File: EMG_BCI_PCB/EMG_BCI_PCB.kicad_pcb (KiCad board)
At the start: 2 copper layers, 94 x 66 mm, 93 parts, among them J1 Conn_01x03, J2 Conn_01x02, J3 Conn_01x03_Male, Q1 Q_PNP_Darlington_BCE, U1 TL072, U2 INA827, U3 ADA4807-4, U4 ADA4807-4, U5 ADS1013IDGS, U6 TC1044S, U7 LM2776

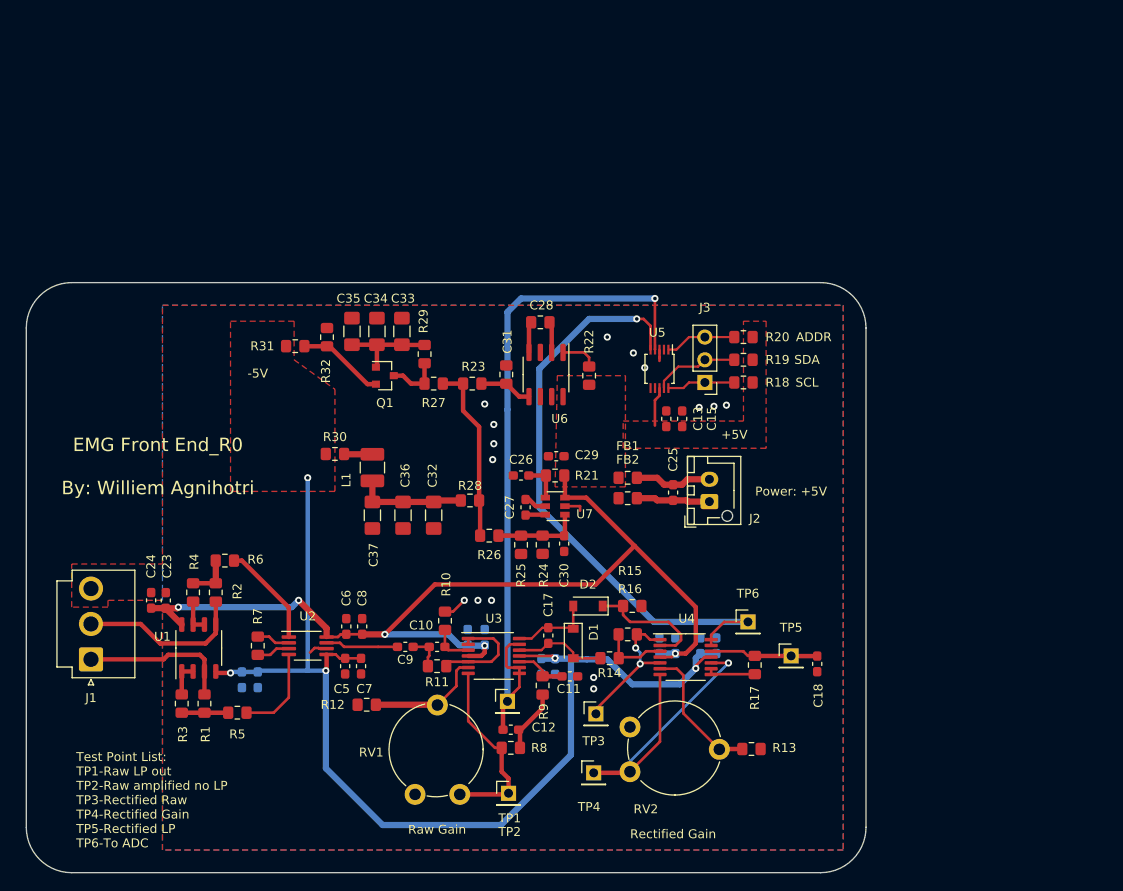
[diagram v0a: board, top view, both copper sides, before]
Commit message: Imported footprints into layout
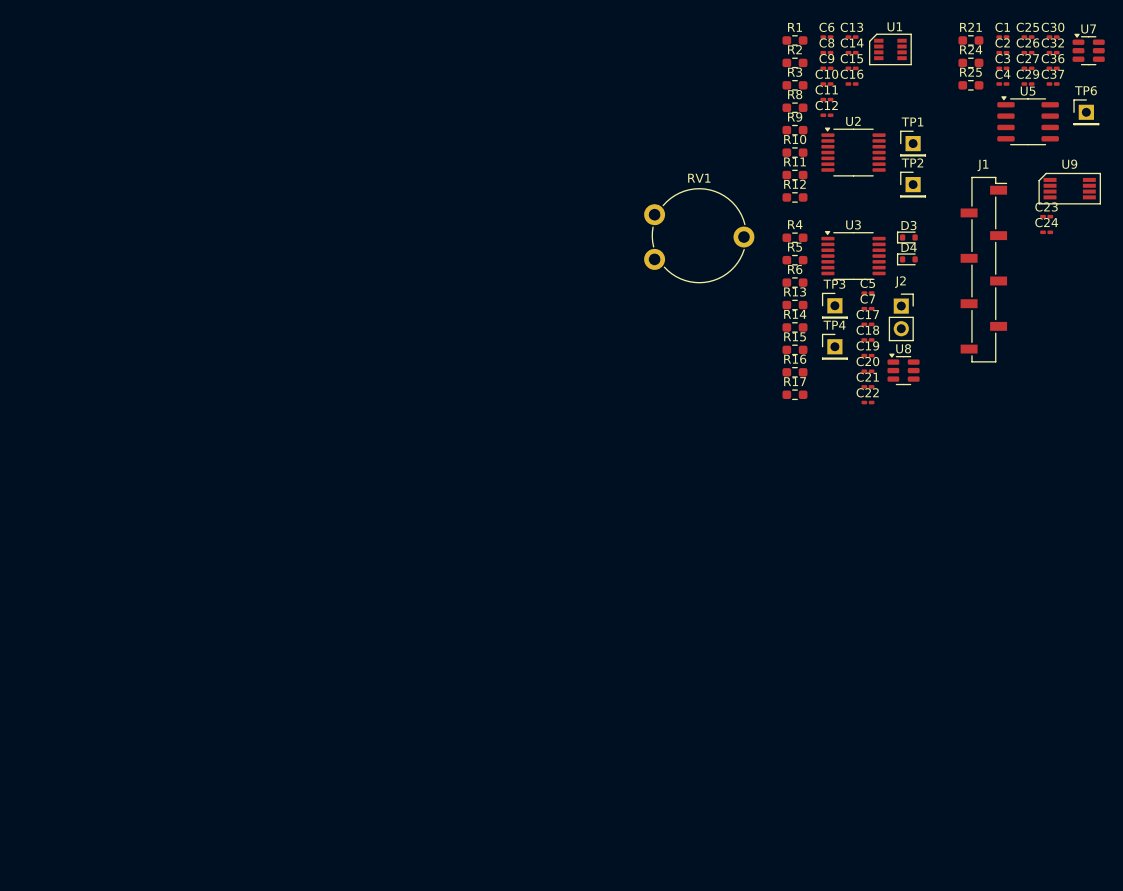
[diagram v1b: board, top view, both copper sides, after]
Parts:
- removed C28, C31: 10uF, Capacitor_SMD:C_0805_2012Metric_Pad1.15x1.40mm_HandSolder
- removed C33, C34, C35: 33u, Capacitor_SMD:C_1206_3216Metric_Pad1.42x1.75mm_HandSolder
- removed D1, D2: BAT42W-V, Diode_SMD:D_SOD-123
- removed FB1, FB2: Ferrite_Bead, Resistor_SMD:R_0805_2012Metric_Pad1.15x1.40mm_HandSolder
- removed J3: Conn_01x03_Male, Connector_PinHeader_2.54mm:PinHeader_1x03_P2.54mm_Vertical
- removed L1: INDUCTOR, Resistor_SMD:R_1210_3225Metric_Pad1.42x2.65mm_HandSolder
- removed Q1: Q_PNP_Darlington_BCE, Package_TO_SOT_SMD:SOT-23
- removed R18, R19, R20, R32: 10K, Resistor_SMD:R_0805_2012Metric_Pad1.15x1.40mm_HandSolder
- removed R22, R23, R26, R27, R28, R30, R31: 0, Resistor_SMD:R_0805_2012Metric_Pad1.15x1.40mm_HandSolder
- removed R29: 1000, Resistor_SMD:R_0805_2012Metric_Pad1.15x1.40mm_HandSolder
- removed R7: 1.6K, Resistor_SMD:R_0805_2012Metric_Pad1.15x1.40mm_HandSolder
- removed RV2: R_POT, Potentiometer_THT:Potentiometer_Piher_PT-10-V10_Vertical
- removed TP5: TestPoint, Connector_PinHeader_2.54mm:PinHeader_1x01_P2.54mm_Vertical
- removed U4: ADA4807-4, Package_SO:TSSOP-14_4.4x5mm_P0.65mm
- removed U6: TC1044S, Package_SO:SOIC-8_3.9x4.9mm_P1.27mm
- added D3: 1N4148WT, Diode_SMD:D_SOD-523, F.Cu at (142.0, 96.5)
- added D4: 1N4148WT, Diode_SMD:D_SOD-523, F.Cu at (142.0, 99.0)
- added U8: MCP1501-18xCH, Package_TO_SOT_SMD:SOT-23-6, F.Cu at (141.4, 111.4)
- added U9: MCP3202, Wills_FootprintLibrary:8-MSOP, F.Cu at (160.0, 91.1)
- C1: value 4.7uF -> 1uF; footprint Capacitor_SMD:C_0603_1608Metric_Pad1.05x0.95mm_HandSolder -> Capacitor_SMD:C_0201_0603Metric_Pad0.64x0.40mm_HandSolder; moved to F.Cu
- C10, C9: value 390n -> 1u; footprint Capacitor_SMD:C_0603_1608Metric_Pad1.05x0.95mm_HandSolder -> Capacitor_SMD:C_0201_0603Metric_Pad0.64x0.40mm_HandSolder
- C11: value 220pF -> 0.0047u; footprint Capacitor_SMD:C_0603_1608Metric_Pad1.05x0.95mm_HandSolder -> Capacitor_SMD:C_0201_0603Metric_Pad0.64x0.40mm_HandSolder
- C12: value 2.2nF -> 0.01u; footprint Capacitor_SMD:C_0603_1608Metric_Pad1.05x0.95mm_HandSolder -> Capacitor_SMD:C_0201_0603Metric_Pad0.64x0.40mm_HandSolder
- C13, C15, C17, C18, C23, C24, C26, C27, C29, C30, C5, C6, C8: footprint Capacitor_SMD:C_0603_1608Metric_Pad1.05x0.95mm_HandSolder -> Capacitor_SMD:C_0201_0603Metric_Pad0.64x0.40mm_HandSolder
- C14, C16, C19, C20, C21, C22: footprint Capacitor_SMD:C_0603_1608Metric_Pad1.05x0.95mm_HandSolder -> Capacitor_SMD:C_0201_0603Metric_Pad0.64x0.40mm_HandSolder; moved to F.Cu
- C2: value 4.7uF -> 1 nF; footprint Capacitor_SMD:C_0603_1608Metric_Pad1.05x0.95mm_HandSolder -> Capacitor_SMD:C_0201_0603Metric_Pad0.64x0.40mm_HandSolder; moved to F.Cu
- C25: value C -> 1uF; footprint Capacitor_SMD:C_0603_1608Metric_Pad1.05x0.95mm_HandSolder -> Capacitor_SMD:C_0201_0603Metric_Pad0.64x0.40mm_HandSolder
- C3, C4: value 0.1uF -> 1uF; footprint Capacitor_SMD:C_0603_1608Metric_Pad1.05x0.95mm_HandSolder -> Capacitor_SMD:C_0201_0603Metric_Pad0.64x0.40mm_HandSolder; moved to F.Cu
- C32, C36, C37: footprint Capacitor_SMD:C_1206_3216Metric_Pad1.42x1.75mm_HandSolder -> Capacitor_SMD:C_0201_0603Metric_Pad0.64x0.40mm_HandSolder
- C7: value 0.1uF -> 4.7uF; footprint Capacitor_SMD:C_0603_1608Metric_Pad1.05x0.95mm_HandSolder -> Capacitor_SMD:C_0201_0603Metric_Pad0.64x0.40mm_HandSolder
- J1: value Conn_01x03 -> Conn_01x08_Pin; footprint Connector_JST:JST_VH_B3P-VH_1x03_P3.96mm_Vertical -> Connector_PinSocket_2.54mm:PinSocket_1x08_P2.54mm_Vertical_SMD_Pin1Right
- J2: value Conn_01x02 -> 2.54 mm header; footprint Connector_JST:JST_XH_B2B-XH-AM_1x02_P2.50mm_Vertical -> Connector_PinSocket_2.54mm:PinSocket_1x02_P2.54mm_Vertical
- R1: value 0 -> 190k; footprint Resistor_SMD:R_0805_2012Metric_Pad1.15x1.40mm_HandSolder -> Resistor_SMD:R_0603_1608Metric_Pad0.98x0.95mm_HandSolder
- R10: value 3.76K -> 22k; footprint Resistor_SMD:R_0805_2012Metric_Pad1.15x1.40mm_HandSolder -> Resistor_SMD:R_0603_1608Metric_Pad0.98x0.95mm_HandSolder
- R11: value 25.6K -> 11k; footprint Resistor_SMD:R_0805_2012Metric_Pad1.15x1.40mm_HandSolder -> Resistor_SMD:R_0603_1608Metric_Pad0.98x0.95mm_HandSolder
- R12: value 2K -> 10k; footprint Resistor_SMD:R_0805_2012Metric_Pad1.15x1.40mm_HandSolder -> Resistor_SMD:R_0603_1608Metric_Pad0.98x0.95mm_HandSolder
- R13, R14, R15, R16, R17, R21, R24, R25: footprint Resistor_SMD:R_0805_2012Metric_Pad1.15x1.40mm_HandSolder -> Resistor_SMD:R_0603_1608Metric_Pad0.98x0.95mm_HandSolder
- R2, R4: value 0 -> 10k; footprint Resistor_SMD:R_0805_2012Metric_Pad1.15x1.40mm_HandSolder -> Resistor_SMD:R_0603_1608Metric_Pad0.98x0.95mm_HandSolder
- R3: value 0 -> 2k; footprint Resistor_SMD:R_0805_2012Metric_Pad1.15x1.40mm_HandSolder -> Resistor_SMD:R_0603_1608Metric_Pad0.98x0.95mm_HandSolder
- R5, R6: value 10K -> 10k; footprint Resistor_SMD:R_0805_2012Metric_Pad1.15x1.40mm_HandSolder -> Resistor_SMD:R_0603_1608Metric_Pad0.98x0.95mm_HandSolder
- R8: value 71.9K -> 56k; footprint Resistor_SMD:R_0805_2012Metric_Pad1.15x1.40mm_HandSolder -> Resistor_SMD:R_0603_1608Metric_Pad0.98x0.95mm_HandSolder
- R9: value 1.29M -> 36k; footprint Resistor_SMD:R_0805_2012Metric_Pad1.15x1.40mm_HandSolder -> Resistor_SMD:R_0603_1608Metric_Pad0.98x0.95mm_HandSolder
- RV1: value R_POT -> R_Potentiometer
- U1: value TL072 -> INA350; footprint Package_SO:SOP-8_3.9x4.9mm_P1.27mm -> Wills_FootprintLibrary:SOT-23-THIN
- U2: value INA827 -> ADA4807-4ARUZ; footprint Package_SO:MSOP-8_3x3mm_P0.65mm -> Package_SO:TSSOP-14_4.4x5mm_P0.65mm
- U3: value ADA4807-4 -> ADA4807-4ARUZ
- U5: value ADS1013IDGS -> MCP1727-3302xSN; footprint Package_SO:TSSOP-10_3x3mm_P0.5mm -> Package_SO:SOIC-8_3.9x4.9mm_P1.27mm
- moved J1 109.0 mm to (150.3, 100.2), turned to 0 degrees
- moved C24 108.4 mm to (157.4, 96.0), turned to 0 degrees
- moved C23 107.5 mm to (157.4, 94.2), turned to 0 degrees
- moved U1 102.4 mm to (139.9, 75.5), turned to 0 degrees
- moved R1 99.4 mm to (129.2, 74.5), turned to 0 degrees
- moved R3 97.5 mm to (129.2, 79.5), turned to 0 degrees
- moved C37 90.2 mm to (158.1, 79.4), turned to 0 degrees
- moved C1 88.7 mm to (152.5, 74.1), turned to 0 degrees
- moved C36 88.3 mm to (158.1, 77.6), turned to 0 degrees
- moved R2 87.8 mm to (129.2, 77.0), turned to 0 degrees
- moved C3 87.4 mm to (152.5, 77.6), turned to 0 degrees
- moved C32 86.5 mm to (158.1, 75.9), turned to 0 degrees
- moved C2 85.9 mm to (152.5, 75.9), turned to 0 degrees
- moved C6 85.1 mm to (132.8, 74.1), turned to 0 degrees
- moved C8 82.6 mm to (132.8, 75.9), turned to 0 degrees
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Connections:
- net /EMG_ADC/AN_1 renamed Net-(U5-PWRGD)
- C1 pad 1: GND -> /Power/Vin+
- C1 pad 2: +5V -> Earth
- C10 pad 1: Net-(C10-Pad1) -> Net-(U2A-+)
- C11 pad 1: GND -> Earth
- C11 pad 2: Net-(C11-Pad2) -> Net-(U2D-+)
- C12 pad 2: /EMG_ADC/AN_0 -> /EMG_FrontEnd/LP_OUT
- C13 pad 1: GND -> Earth
- C13 pad 2: +5V -> +3.3V
- C14 pad 1: GND -> Earth
- C14 pad 2: -5V -> -3V3
- C15 pad 1: GND -> Earth
- C15 pad 2: +5V -> +3.3V
- C16 pad 1: GND -> Earth
- C16 pad 2: -5V -> -3V3
- C17 pad 1: Net-(C17-Pad1) -> Net-(D3-A)
- C17 pad 2: Net-(C17-Pad2) -> Net-(D3-K)
- C18 pad 1: Net-(C18-Pad1) -> /EMG_ADC/AdcCh1
- C18 pad 2: GND -> Earth
- C19 pad 1: +5V -> +3.3V
- C19 pad 2: GND -> Earth
- C2 pad 1: GND -> Net-(U5-Cdelay)
- C2 pad 2: -5V -> Earth
- C20 pad 1: -5V -> -3V3
- C20 pad 2: GND -> Earth
- C21 pad 1: +5V -> +3.3V
- C21 pad 2: GND -> Earth
- C22 pad 1: -5V -> -3V3
- C22 pad 2: GND -> Earth
- C23 pad 1: +5V -> +3.3V
- C23 pad 2: GND -> Earth
- C24 pad 1: +5V -> +3.3V
- C24 pad 2: GND -> Earth
- C25 pad 2: /Power/WGND -> Earth
- C26 pad 2: GND -> Earth
- C29 pad 1: +5V -> +3.3V
- C29 pad 2: GND -> Earth
- C3 pad 1: GND -> +3.3V
- C3 pad 2: +5V -> Earth
- C30 pad 1: Net-(C30-Pad1) -> -3V3
- C30 pad 2: GND -> Earth
- C32 pad 1: Net-(C32-Pad1) -> -3V3
- C32 pad 2: GND -> Earth
- C36 pad 1: Net-(C32-Pad1) -> -3V3
- C36 pad 2: GND -> Earth
- C37 pad 1: Net-(C32-Pad1) -> -3V3
- C37 pad 2: GND -> Earth
- C4 pad 1: GND -> +3.3V
- C4 pad 2: -5V -> Earth
- C5 pad 1: -5V -> Earth
- C5 pad 2: GND -> +3.3V
- C6 pad 1: GND -> Earth
- C6 pad 2: +5V -> +3.3V
- C7 pad 1: -5V -> Earth
- C7 pad 2: GND -> Net-(U8-OUT)
- C8 pad 1: GND -> Earth
- C8 pad 2: +5V -> +3.3V
- J1 pad 1: /EMG_FrontEnd/Trode+ -> /EMG_FrontEnd/Electrode+
- J1 pad 2: /EMG_FrontEnd/Trode- -> /EMG_FrontEnd/Electrode-
- J1 pad 3: GND -> /Power/Vin+
- J2 pad 1: /Power/WGND -> /EMG_ADC/AdcCh1
- J2 pad 2: /Power/Vin+ -> /EMG_ADC/AdcCh0
- R1 pad 1: /EMG_FrontEnd/ALT+ -> Net-(R1-Pad1)
- R1 pad 2: /EMG_FrontEnd/Trode+ -> Net-(U2B--)
- R10 pad 1: Net-(C10-Pad1) -> Net-(U2A-+)
- R10 pad 2: GND -> Earth
- R11 pad 1: Net-(R11-Pad1) -> Net-(U2A--)
- R12 pad 1: Net-(R12-Pad1) -> Net-(U2B--)
- R12 pad 2: GND -> Earth
- R13 pad 1: Net-(R13-Pad1) -> Net-(U3C--)
- R13 pad 2: GND -> Earth
- R14 pad 1: Net-(R14-Pad1) -> Net-(U3B-+)
- R14 pad 2: Net-(C17-Pad1) -> Net-(D3-A)
- R15 pad 1: GND -> Earth
- R15 pad 2: Net-(D2-Pad1) -> Net-(D4-K)
- R16 pad 1: Net-(R16-Pad1) -> Net-(U3C-+)
- R16 pad 2: Net-(R14-Pad1) -> Net-(U3B-+)
- R17 pad 1: Net-(C18-Pad1) -> /EMG_ADC/AdcCh1
- R2 pad 1: /EMG_FrontEnd/ALT- -> +3.3V
- R2 pad 2: /EMG_FrontEnd/Trode- -> Net-(U2C-+)
- R21 pad 1: +5V -> +3.3V
- R24 pad 1: Net-(C30-Pad1) -> -3V3
- R24 pad 2: GND -> Earth
- R25 pad 1: Net-(C30-Pad1) -> -3V3
- R25 pad 2: GND -> Earth
- R3 pad 1: /EMG_FrontEnd/ALT+ -> Net-(U2C-+)
- R3 pad 2: Net-(R3-Pad2) -> Earth
- R4 pad 1: /EMG_FrontEnd/ALT- -> Net-(U3D--)
- R4 pad 2: Net-(R4-Pad2) -> /EMG_FrontEnd/LP_OUT
- R5 pad 1: Net-(R5-Pad1) -> /EMG_ADC/AdcCh0
- R5 pad 2: /EMG_FrontEnd/ALT+ -> Net-(U3D--)
- R6 pad 1: Net-(R6-Pad1) -> Net-(U3D--)
- R6 pad 2: /EMG_FrontEnd/ALT- -> Net-(U8-OUT)
- R8 pad 2: Net-(R8-Pad2) -> Net-(R1-Pad1)
- R9 pad 1: Net-(C11-Pad2) -> Net-(U2D-+)
- RV1 pad 1: Net-(R8-Pad2) -> Net-(R17-Pad2)
- RV1 pad 2: Net-(R12-Pad1) -> Net-(U3C--)
- RV1 pad 3: Net-(RV1-Pad3) -> unconnected-(RV1-Pad3)
- TP1 pad 1: /EMG_ADC/AN_0 -> /EMG_FrontEnd/LP_OUT
- TP2 pad 1: Net-(R8-Pad2) -> Net-(R1-Pad1)
- TP3 pad 1: Net-(R16-Pad1) -> Net-(U3C-+)
- TP4 pad 1: Net-(RV2-Pad1) -> Net-(R17-Pad2)
- U1 pad 1: Net-(R3-Pad2) -> +3.3V
- U1 pad 2: Net-(R3-Pad2) -> /EMG_FrontEnd/Electrode-
- U1 pad 3: /EMG_FrontEnd/Trode+ -> /EMG_FrontEnd/Electrode+
- U1 pad 4: -5V -> Earth
- U1 pad 5: /EMG_FrontEnd/Trode- -> Net-(U1-Ref)
- U1 pad 6: Net-(R4-Pad2) -> Net-(C9-Pad2)
- U1 pad 7: Net-(R4-Pad2) -> +3.3V
- U1 pad 8: +5V -> +3.3V
- U2 pad 1: Net-(R6-Pad1) -> Net-(U2A--)
- U2 pad 2: Net-(R7-Pad1) -> Net-(U2A--)
- U2 pad 3: Net-(R7-Pad2) -> Net-(U2A-+)
- U2 pad 4: Net-(R5-Pad1) -> +3.3V
- U2 pad 5: -5V -> Net-(U2A--)
- U2 pad 6: GND -> Net-(U2B--)
- U2 pad 7: Net-(C9-Pad2) -> Net-(R1-Pad1)
- U2 pad 8: +5V -> Net-(U1-Ref)
- U3 pad 1: Net-(R11-Pad1) -> Net-(D3-K)
- U3 pad 10: Net-(C11-Pad2) -> Net-(U3C-+)
- U3 pad 11: -5V -> -3V3
- U3 pad 12: Net-(C17-Pad1) -> Earth
- U3 pad 13: /EMG_ADC/AN_0 -> Net-(U3D--)
- U3 pad 14: Net-(C17-Pad2) -> /EMG_ADC/AdcCh0
- U3 pad 2: Net-(R11-Pad1) -> /EMG_FrontEnd/LP_OUT
- U3 pad 3: Net-(C10-Pad1) -> Net-(D3-A)
- U3 pad 4: +5V -> +3.3V
- U3 pad 5: Net-(R11-Pad1) -> Net-(U3B-+)
- U3 pad 6: Net-(R12-Pad1) -> Net-(D4-K)
- U3 pad 7: Net-(R8-Pad2) -> Net-(U3C-+)
- U3 pad 8: /EMG_ADC/AN_0 -> Net-(R17-Pad2)
- U3 pad 9: /EMG_ADC/AN_0 -> Net-(U3C--)
- U5 pad 1: /EMG_ADC/ADDR -> /Power/Vin+
- U5 pad 2: Net-(U5-Pad2) -> /Power/Vin+
- U5 pad 3: GND -> /Power/Vin+
- U5 pad 4: /EMG_ADC/AN_0 -> Earth
- U5 pad 6: Net-(U5-Pad6) -> Net-(U5-Cdelay)
- U5 pad 7: Net-(U5-Pad7) -> +3.3V
- U5 pad 8: +5V -> +3.3V
- U7 pad 1: Net-(C30-Pad1) -> -3V3
- U7 pad 2: GND -> Earth
- U7 pad 3: +5V -> +3.3V
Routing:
- net -5V: track 124.3 -> 0.00 mm, vias 5 -> 0
- net +5V: track 115.0 -> 0.00 mm, vias 5 -> 0
- net /EMG_ADC/AN_0: track 79.3 -> 0.00 mm, vias 1 -> 0
- net Net-(U5-PWRGD): track 67.8 -> 0.00 mm, vias 1 -> 0
- net Net-(RV2-Pad1): track 35.1 -> 0.00 mm, vias 1 -> 0
- net Net-(R8-Pad2): track 21.2 -> 0.00 mm
- net Net-(R23-Pad1): track 20.1 -> 0.00 mm
- net /EMG_FrontEnd/Trode-: track 18.9 -> 0.00 mm
- net /EMG_FrontEnd/Trode+: track 17.0 -> 0.00 mm
- net Net-(R16-Pad1): track 16.3 -> 0.00 mm, vias 2 -> 0
- net Net-(R13-Pad1): track 15.5 -> 0.00 mm
- net Net-(D2-Pad1): track 13.9 -> 0.00 mm
- net Net-(R12-Pad1): track 13.1 -> 0.00 mm
- net Net-(C32-Pad1): track 12.3 -> 0.00 mm
- net Net-(C18-Pad1): track 12.1 -> 0.00 mm
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- removed copper zone on F.Cu, net +5V
- removed copper zone on F.Cu, net -5V
- removed copper zone on B.Cu, net GND
- removed copper zone on F.Cu, net GND
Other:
- board outline removed
- net class Default removed
- board text removed: "+5V"
- board text removed: "-5V"
- board text removed: "ADDR"
- board text removed: "EMG Front End_R0 By: Williem Agnihotri"
- board text removed: "Power: +5V"
- board text removed: "Raw Gain"
- board text removed: "Rectified Gain"
- board text removed: "SCL"
- board text removed: "SDA"
- board text removed: "Test Point List: TP1-Raw LP out TP2-Raw amplified no LP TP3-Rectified Raw TP4-Rectified Gain TP5-Rectified LP TP6-To ADC"
